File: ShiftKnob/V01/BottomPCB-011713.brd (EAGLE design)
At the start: 37.8 x 40.2 mm, 39 parts, among them IC2 7805DT, Q1 16MHz, Q2 MOSFET-NCHANNELSMD, Q3 MOSFET-NCHANNELSMD, Q4 MOSFET-NCHANNELSMD, Q5 MOSFET-NCHANNELSMD, Q6 MOSFET-NCHANNELSMD, U1 ATMEGA328

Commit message: attach button to arduino pin 2 rather than 12 to use internal interrupt. adjust board accordingly. remove resistor and use internal resistor of atemga328.
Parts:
- removed R12: 10k, SparkFun-Passives:0402-RES
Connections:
- net D12: no longer R12.1, S1.3, S1.4
- net D2: now also S1.3, S1.4
- net VCC: no longer R12.2
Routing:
- net D12: track 25.7 -> 0.00 mm, vias 2 -> 0
- net D2: track 0.00 -> 16.6 mm
- net VCC: track 89.2 -> 88.2 mm
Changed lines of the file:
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@@
 <setting verticaltext="up"/>
 </settings>
-<grid distance="0.05" unitdist="inch" unit="inch" style="lines" multiple="1" display="yes" altdistance="0.025" altunitdist="inch" altunit="inch"/>
+<grid distance="0.001" unitdist="inch" unit="inch" style="lines" multiple="1" display="yes" altdistance="0.025" altunitdist="inch" altunit="inch"/>
 <layers>
 <layer number="1" name="Top" color="4" fill="1" visible="yes" active="yes"/>
@@
 <wire x1="30.2006" y1="13.8684" x2="32.6644" y2="13.8684" width="0.4064" layer="22"/>
 <wire x1="18.0086" y1="7.2898" x2="18.0086" y2="9.1186" width="0.4064" layer="21"/>
-<wire x1="15.24" y1="39.37" x2="15.24" y2="41.91" width="0.2032" layer="20"/>
-<wire x1="27.94" y1="39.37" x2="27.94" y2="41.91" width="0.2032" layer="20"/>
-<wire x1="15.24" y1="41.91" x2="27.94" y2="41.91" width="0.2032" layer="20" curve="-34.708049"/>
-<wire x1="15.24" y1="39.37" x2="27.94" y2="39.37" width="0.2032" layer="20" curve="320.692352"/>
+<wire x1="15.24" y1="39.37" x2="15.24" y2="41.91" width="0.254" layer="20"/>
+<wire x1="27.94" y1="39.37" x2="27.94" y2="41.91" width="0.254" layer="20"/>
+<wire x1="15.24" y1="41.91" x2="27.94" y2="41.91" width="0.254" layer="20" curve="-34.708049"/>
+<wire x1="15.24" y1="39.37" x2="27.94" y2="39.37" width="0.254" layer="20" curve="320.692352"/>
 </plain>
 <attributes>
@@
 <element name="Q5" library="SparkFun-DiscreteSemi" package="SOT23-3" value="MOSFET-NCHANNELSMD" x="15.306" y="20.64" rot="R270"/>
 <element name="Q6" library="SparkFun-DiscreteSemi" package="SOT23-3" value="MOSFET-NCHANNELSMD" x="15.306" y="23.942" rot="R270"/>
-<element name="R12" library="SparkFun-Passives" package="0402-RES" value="10k" x="12.131" y="18.1" rot="R90"/>
 <element name="D2" library="diode" package="SOD123" value="MBR0520LT" x="31.943" y="11.1404" rot="MR135"/>
 </elements>
@@
 <contactref element="LED1" pad="A"/>
 <wire x1="7.624" y1="20.156" x2="7.878" y2="20.578" width="0.4064" layer="1"/>
-<contactref element="R12" pad="2"/>
 <wire x1="7.624" y1="20.156" x2="7.624" y2="21.34" width="0.4064" layer="1"/>
 <wire x1="7.624" y1="21.34" x2="8.575" y2="22.291" width="0.4064" layer="1"/>
@@
 <wire x1="24.2468" y1="34.5846" x2="23.8472875" y2="34.4322" width="0.4064" layer="1"/>
 <wire x1="23.8472875" y1="34.4322" x2="23.32316875" y2="33.93348125" width="0.4064" layer="1"/>
-<wire x1="12.131" y1="18.75" x2="12.131" y2="19.751" width="0.254" layer="1"/>
 <wire x1="12.131" y1="19.751" x2="13.02" y2="20.64" width="0.254" layer="1"/>
 <wire x1="28.006" y1="22.525" x2="28.012" y2="22.519" width="0.8128" layer="1"/>
@@
 <signal name="D12">
 <contactref element="U1" pad="16"/>
-<contactref element="S1" pad="3"/>
-<contactref element="S1" pad="4"/>
-<contactref element="R12" pad="1"/>
-<wire x1="12.131" y1="17.45" x2="12.131" y2="17.084" width="0.254" layer="1"/>
-<wire x1="12.131" y1="17.084" x2="13.02" y2="16.195" width="0.254" layer="1"/>
-<via x="13.02" y="16.195" extent="1-16" drill="0.5" diameter="0.4064"/>
-<via x="18.6334" y="19.3192" extent="1-16" drill="0.5" diameter="0.4064"/>
-<wire x1="20.005" y1="26.99" x2="15.139575" y2="31.982425" width="0.254" layer="1"/>
-<wire x1="15.139575" y1="31.982425" x2="14.989771875" y2="32.236425" width="0.254" layer="1"/>
-<wire x1="19.685" y1="24.13" x2="20.005" y2="24.577" width="0.254" layer="1"/>
-<wire x1="20.005" y1="24.577" x2="20.005" y2="26.99" width="0.254" layer="1"/>
-<wire x1="18.6334" y1="19.3192" x2="18.1" y2="19.878" width="0.254" layer="1"/>
-<wire x1="18.1" y1="19.878" x2="18.1" y2="22.672" width="0.254" layer="1"/>
-<wire x1="18.1" y1="22.672" x2="19.558" y2="24.13" width="0.254" layer="1"/>
-<wire x1="19.558" y1="24.13" x2="19.685" y2="24.13" width="0.254" layer="1"/>
-<wire x1="18.6334" y1="19.3192" x2="18.928" y2="19.05" width="0.254" layer="1"/>
-<wire x1="18.928" y1="19.05" x2="19.685" y2="19.05" width="0.254" layer="1"/>
-<wire x1="13.02" y1="16.195" x2="15.5092" y2="16.195" width="0.3048" layer="16"/>
-<wire x1="15.5092" y1="16.195" x2="18.6334" y2="19.3192" width="0.3048" layer="16"/>
 </signal>
 <signal name="D11">
@@
 <signal name="D2">
 <contactref element="U1" pad="32"/>
+<contactref element="S1" pad="3"/>
+<contactref element="S1" pad="4"/>
+<wire x1="19.685" y1="24.13" x2="19.7612" y2="24.13" width="0.254" layer="1"/>
+<wire x1="23.3426" y1="30.9118" x2="24.2062" y2="30.9118" width="0.254" layer="1"/>
+<wire x1="24.2062" y1="30.9118" x2="24.992428125" y2="30.125571875" width="0.254" layer="1"/>
+<wire x1="24.992428125" y1="30.125571875" x2="25.020225" y2="30.125571875" width="0.254" layer="1"/>
+<wire x1="18.3134" y1="22.7584" x2="19.685" y2="24.13" width="0.254" layer="1"/>
+<wire x1="19.7104" y1="19.0246" x2="18.3134" y2="20.4216" width="0.254" layer="1"/>
+<wire x1="18.3134" y1="22.7584" x2="18.3134" y2="20.4216" width="0.254" layer="1"/>
+<wire x1="23.3426" y1="30.9118" x2="19.9898" y2="27.559" width="0.254" layer="1"/>
+<wire x1="19.9898" y1="27.559" x2="19.9898" y2="25.7048" width="0.254" layer="1"/>
+<wire x1="19.9898" y1="25.7048" x2="19.685" y2="25.4" width="0.254" layer="1"/>
+<wire x1="19.685" y1="25.4" x2="19.685" y2="24.13" width="0.254" layer="1"/>
+<wire x1="19.7104" y1="19.0246" x2="19.685" y2="19.05" width="0" layer="19" extent="1-1"/>
 </signal>
 <signal name="D3">

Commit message: final finalized versions of boards and fab files.
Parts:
- moved U$3 3.64 mm to (20.0, 26.5)
- moved U$11 2.32 mm to (15.8, 27.9)
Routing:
- net VCC: track 88.2 -> 86.4 mm
- net GND: track 30.1 -> 28.5 mm
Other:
- board text added: "2-07-13"
- board text removed: "1-28-13"

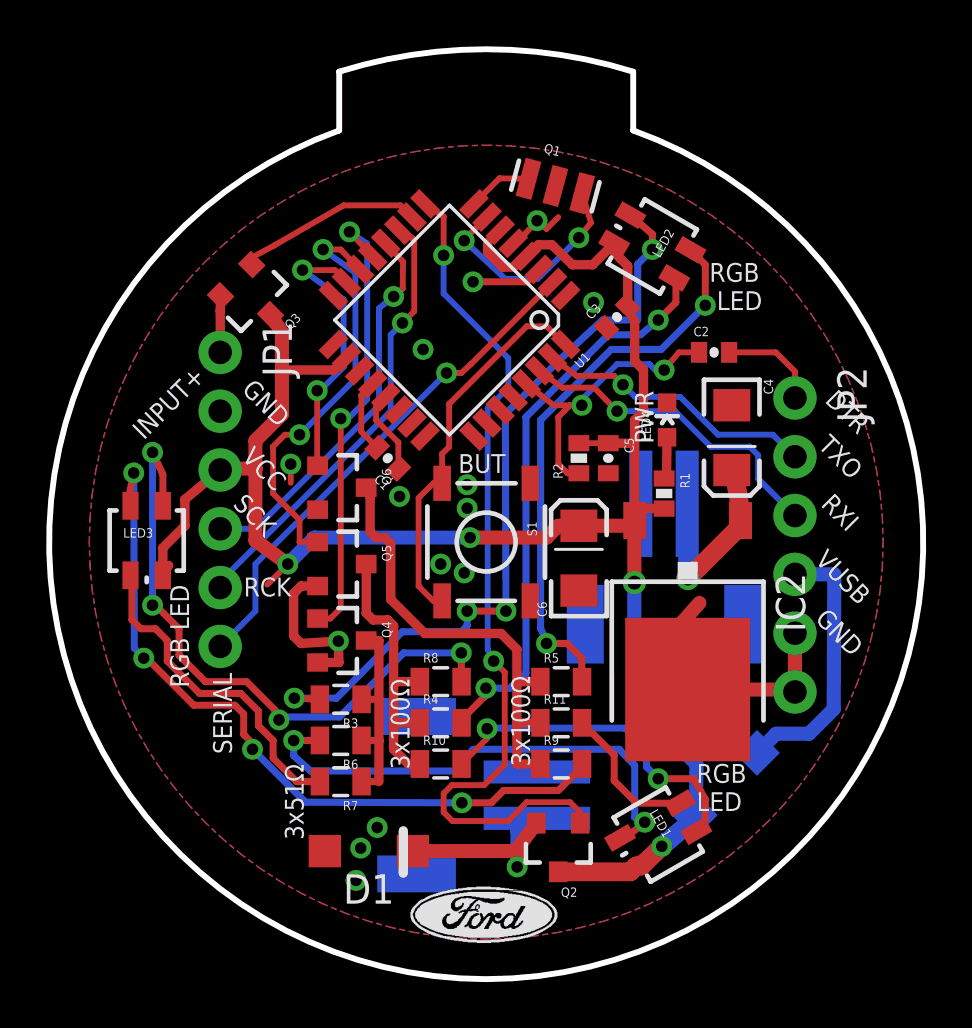
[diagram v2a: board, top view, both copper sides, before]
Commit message: fix board layout and schematic to properly setup MOSFETs. regenerate Gerber files. Change N-Channel MOSFET to P-Channel for 7segment brightness control (INPUT+)
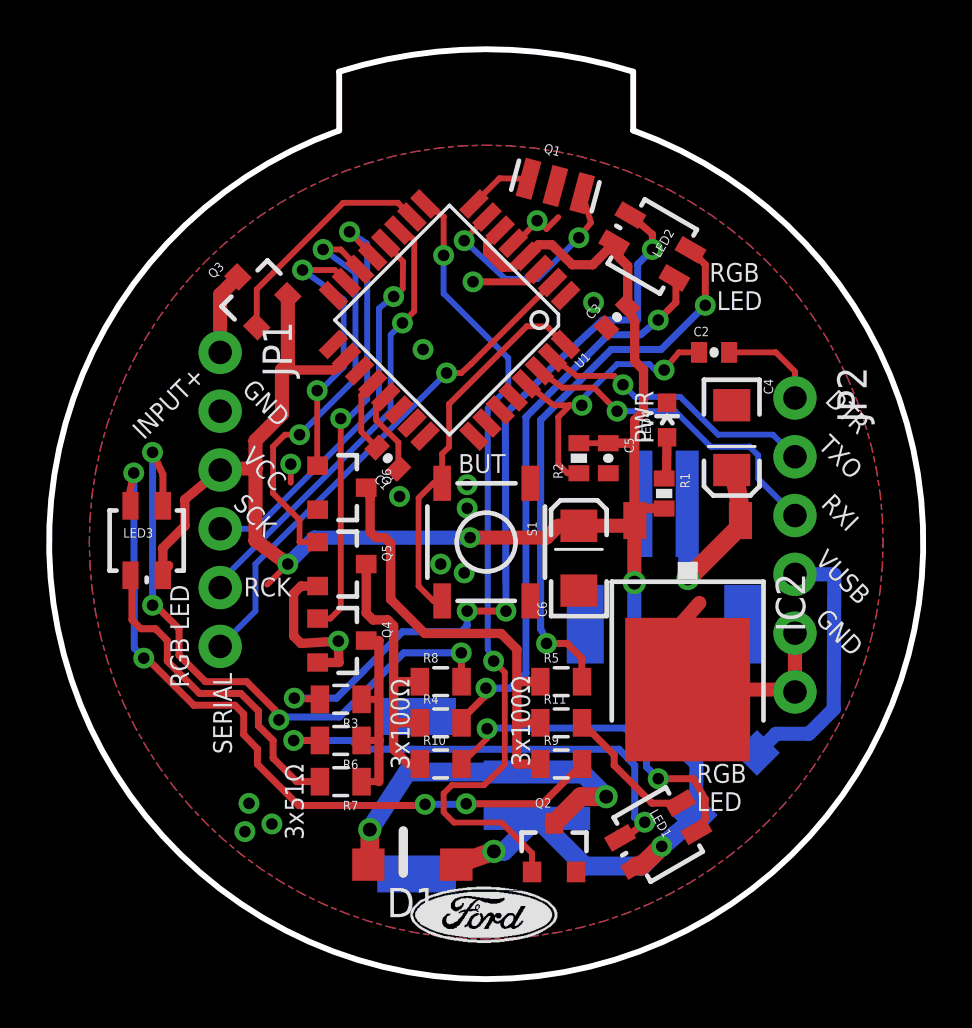
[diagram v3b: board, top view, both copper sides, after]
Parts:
- Q3: value MOSFET-NCHANNELSMD -> MOSFET-PCHANNELSMD
- moved D1 1.97 mm to (18.4, 7.66)
- moved Q2 0.21 mm to (24.5, 8.34), turned to 0 degrees
- moved Q3 0.16 mm to (11.6, 32.3), turned to 45 degrees
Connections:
- removed net MOTOR+: D1.C, JP4.2, Q2.2
- new net MOTOR-: D1.A, JP4.1, Q2.3
- net GND: now also Q2.2; no longer D1.A, JP4.1
- net INPUT+: now also Q3.3; no longer Q3.2
- net VCC: now also D1.C, JP4.2, Q3.2; no longer Q2.3, Q3.3
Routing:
- net MOTOR-: track 0.00 -> 16.2 mm, vias 0 -> 2
- net MOTOR+: track 9.28 -> 0.00 mm, vias 1 -> 0
- net VCC: track 86.4 -> 94.5 mm, vias 4 -> 5
- net D6/INPUT+: track 8.02 -> 10.1 mm
- net D5/MOTOR: track 37.4 -> 35.8 mm
- net N$9: track 21.7 -> 20.4 mm
- net INPUT+: track 2.45 -> 3.58 mm

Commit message: update schematics with new Ford frame.
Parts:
- removed U$11: LOGO-SFESK, SparkFun:SFE-LOGO-FLAME
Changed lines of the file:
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@@
 <element name="C3" library="SparkFun" package="0402-CAP" value="0.1uF" x="27.244" y="31.308" rot="R45"/>
 <element name="C1" library="SparkFun" package="0402-CAP" value="0.1uF" x="17.338" y="25.212" rot="R135"/>
-<element name="U$11" library="SparkFun" package="SFE-LOGO-FLAME" value="LOGO-SFESK" x="15.814" y="27.879" smashed="yes" rot="MR90"/>
 <element name="Q1" library="SparkFun" package="RESONATOR-SMD" value="16MHz" x="24.577" y="36.9722" rot="R345"/>
 <element name="U1" library="SparkFun" package="TQFP32-08" value="ATMEGA328" x="20.005" y="31.181" rot="R225"/>

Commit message: update with new frames and printed drawings for assembly.
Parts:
- added U$1: (no value), FORD_frames:DOCFIELD
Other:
- board text added: "01"
- board text added: "Zachary Nelson znelson1@ford.com"
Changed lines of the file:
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@@
 <setting verticaltext="up"/>
 </settings>
-<grid distance="0.001" unitdist="inch" unit="inch" style="lines" multiple="1" display="yes" altdistance="0.025" altunitdist="inch" altunit="inch"/>
+<grid distance="0.05" unitdist="inch" unit="inch" style="lines" multiple="1" display="yes" altdistance="0.025" altunitdist="inch" altunit="inch"/>
 <layers>
 <layer number="1" name="Top" color="4" fill="1" visible="yes" active="yes"/>
@@
 <layer number="46" name="Milling" color="3" fill="1" visible="no" active="yes"/>
 <layer number="47" name="Measures" color="7" fill="1" visible="yes" active="yes"/>
-<layer number="48" name="Document" color="7" fill="1" visible="no" active="yes"/>
+<layer number="48" name="Document" color="7" fill="1" visible="yes" active="yes"/>
 <layer number="49" name="Reference" color="7" fill="1" visible="no" active="yes"/>
 <layer number="50" name="dxf" color="7" fill="1" visible="no" active="no"/>
@@
 <layer number="150" name="Notes" color="7" fill="1" visible="yes" active="yes"/>
 <layer number="151" name="HeatSink" color="7" fill="1" visible="yes" active="yes"/>
+<layer number="175" name="transfer" color="13" fill="1" visible="yes" active="yes"/>
 <layer number="199" name="Contour" color="7" fill="1" visible="no" active="yes"/>
 <layer number="200" name="200bmp" color="1" fill="10" visible="yes" active="yes"/>
@@
 <wire x1="15.24" y1="41.91" x2="27.94" y2="41.91" width="0.254" layer="20" curve="-34.708049"/>
 <wire x1="15.24" y1="39.37" x2="27.94" y2="39.37" width="0.254" layer="20" curve="320.692352"/>
+<text x="17.78" y="-41.91" size="3.81" layer="48">Zachary Nelson
+znelson1@ford.com</text>
+<text x="93.98" y="-40.64" size="3.81" layer="48">01</text>
+<wire x1="-46.99" y1="-19.05" x2="-46.99" y2="60.96" width="0.1016" layer="48"/>
+<wire x1="-46.99" y1="60.96" x2="105.41" y2="60.96" width="0.1016" layer="48"/>
+<wire x1="105.41" y1="60.96" x2="105.41" y2="-19.05" width="0.1016" layer="48"/>
+<dimension x1="21.59" y1="21.59" x2="40.10355" y2="25.291265625" x3="47.75219375" y3="26.8204" layer="48" dtype="radius"/>
+<dimension x1="21.59" y1="21.59" x2="18.825234375" y2="42.6987875" x3="17.812265625" y3="50.43273125" layer="48" dtype="radius"/>
+<dimension x1="15.24" y1="41.91" x2="27.94" y2="41.91" x3="21.59" y3="48.26" layer="48"/>
 </plain>
 <attributes>
@@
 <element name="Q6" library="SparkFun-DiscreteSemi" package="SOT23-3" value="MOSFET-NCHANNELSMD" x="15.306" y="23.942" rot="R270"/>
 <element name="D2" library="diode" package="SOD123" value="MBR0520LT" x="31.943" y="11.1404" rot="MR135"/>
+<element name="U$1" library="FORD_frames" package="DOCFIELD" value="" x="-46.99" y="-49.53"/>
 </elements>
 <signals>
